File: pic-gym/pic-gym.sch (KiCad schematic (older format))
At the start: 27 parts, among them CON1 BARREL_JACK, SW1 SW_SPST, SW2 SW_Push, SW3 SW_DIP_x05, U1 LM7805, U2 PIC16F84A-XX/P, Y1 4MHz

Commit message: Netlist Exported
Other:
- note added: "POWER"
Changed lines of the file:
@@
 Wire Wire Line
 	5850 6400 5850 6500
+Wire Notes Line
+	6150 5700 6150 7250
+Wire Notes Line
+	6150 7250 1350 7250
+Wire Notes Line
+	1350 7250 1350 5700
+Wire Notes Line
+	1350 5700 6150 5700
+Text Notes 1500 5850 0    60   ~ 0
+POWER
 $EndSCHEMATC

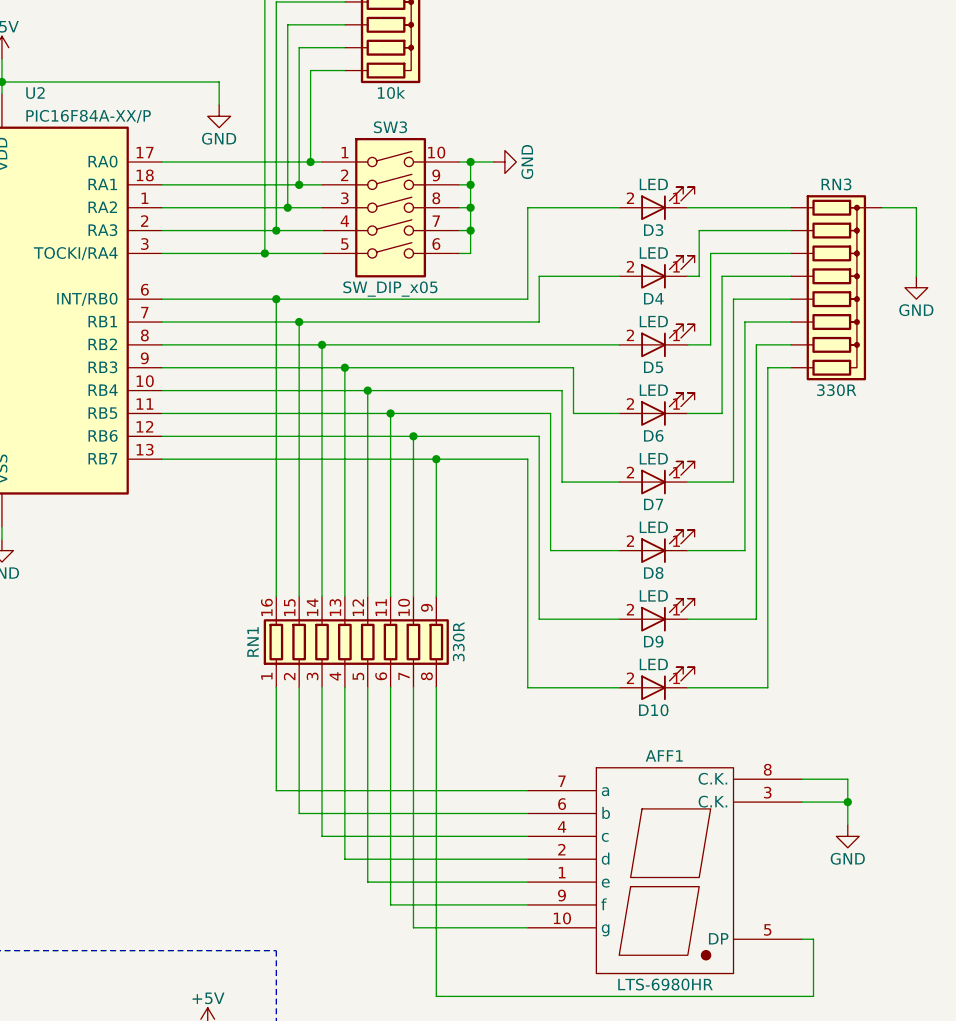
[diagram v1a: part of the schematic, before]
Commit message: Resistor arrays changed
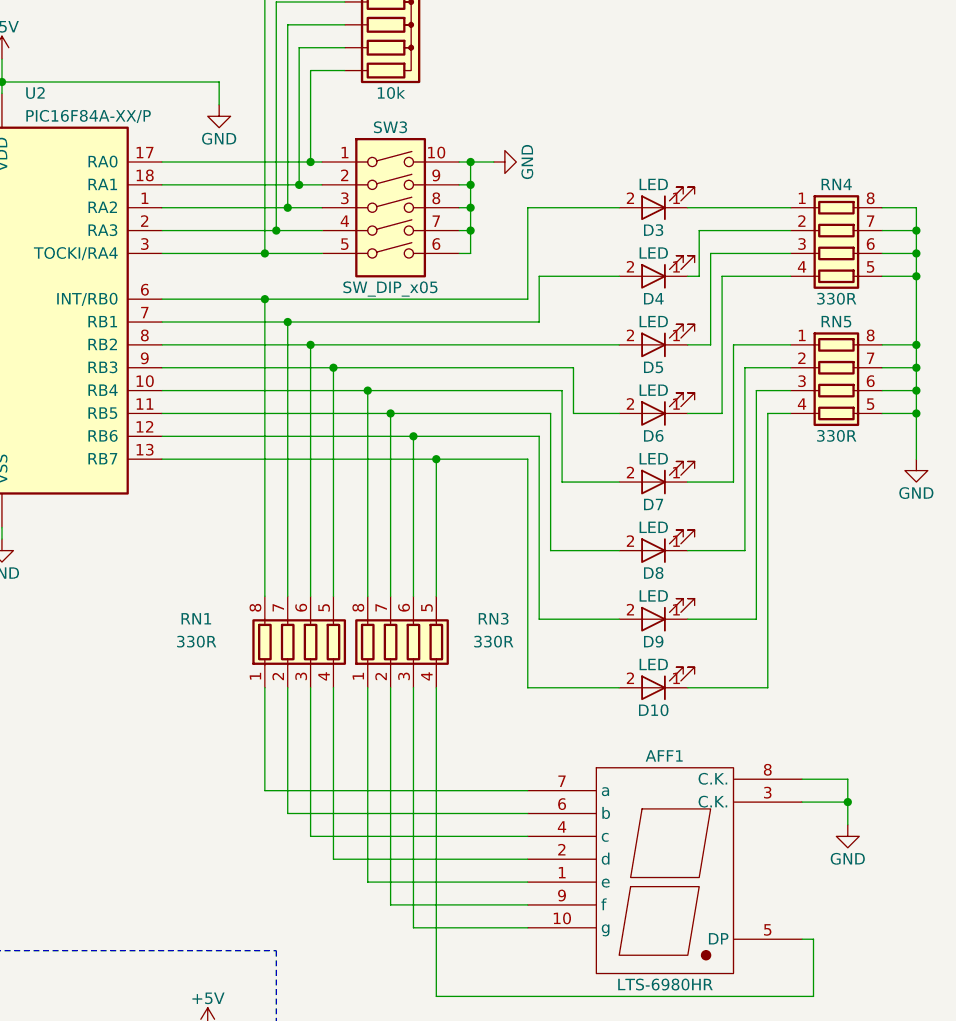
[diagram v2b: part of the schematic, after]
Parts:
- removed RN1: 330R, symbol R_Pack08
- removed RN3: 330R, Resistors_ThroughHole:R_Array_SIP9, symbol R_Network08
- added RN1, RN3, RN4, RN5: 330R, symbol R_Pack04
- AFF1: footprint (none) -> Displays_7-Segment:7SegmentLED_LTS6760_LTS6780
- C1, C2, C3: footprint (none) -> Capacitors_SMD:C_0805_HandSoldering
- C4, C5: footprint (none) -> Capacitors_THT:C_Radial_D5_L11_P2
- CON1: footprint (none) -> Connectors:JACK_ALIM
- D1: footprint Diodes_ThroughHole:D_DO-41_SOD81_Horizontal_RM10 -> Diodes_THT:Diode_DO-35_SOD27_Horizontal_RM10
- D10, D2, D3, D4, D5, D6, D7, D8, D9: footprint (none) -> LEDs:LED-3MM
- R1: footprint (none) -> Resistors_THT:Resistor_Horizontal_RM10mm
- U2: footprint (none) -> Housings_DIP:DIP-18_W7.62mm_LongPads
- Y1: footprint (none) -> Crystals:HC-49V
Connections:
- net +5V: now also RN4.5 (R4.2), RN4.6 (R3.2), RN4.7 (R2.2), RN4.8 (R1.2), RN5.5 (R4.2), RN5.6 (R3.2), RN5.7 (R2.2), RN5.8 (R1.2)
- net at D7.2 (A), U2.10 (RB4): now also RN3.8 (R1.2)
- net at D8.2 (A), U2.11 (RB5): now also RN3.7 (R2.2)
- net at D9.2 (A), U2.12 (RB6): now also RN3.6 (R3.2)
- net at D10.2 (A), U2.13 (RB7): now also RN3.5 (R4.2)
- net at D3.2 (A), U2.6 (INT/RB0): now also RN1.8 (R1.2)
- net at D4.2 (A), U2.7 (RB1): now also RN1.7 (R2.2)
- net at D5.2 (A), U2.8 (RB2): now also RN1.6 (R3.2)
- net at D6.2 (A), U2.9 (RB3): now also RN1.5 (R4.2)
- net at D6.1 (K): now also RN4.4 (R4.1)
- net at D7.1 (K): now also RN5.1 (R1.1)
- net at D3.1 (K): now also RN4.1 (R1.1)
- net at D4.1 (K): now also RN4.2 (R2.1)
- net at D5.1 (K): now also RN4.3 (R3.1)
- net at D8.1 (K): now also RN5.2 (R2.1)
- net at D9.1 (K): now also RN5.3 (R3.1)
- net at D10.1 (K): now also RN5.4 (R4.1)
- net at AFF1.7 (a): now also RN1.1 (R1.1)
- net at AFF1.6 (b): now also RN1.2 (R2.1)
- net at AFF1.4 (c): now also RN1.3 (R3.1)
- net at AFF1.2 (d): now also RN1.4 (R4.1)
- net at AFF1.1 (e): now also RN3.1 (R1.1)
- net at AFF1.9 (f): now also RN3.2 (R2.1)
- net at AFF1.10 (g): now also RN3.3 (R3.1)
- net at AFF1.5 (DP): now also RN3.4 (R4.1)
